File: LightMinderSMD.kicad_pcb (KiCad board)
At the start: 2 copper layers, 49.5 x 23 mm, 41 parts, among them J1 Conn_01x04_Female, J2 AVR-ISP-6, J3 Conn_01x04, J4 Conn_01x02_Female, Q1 Q_NPN_BEC, Q2 Q_NPN_BEC, Q3 STD35P6LLF6, U1 ATmega328P-AU, U2 LM3480-3.3, Y1 Crystal_GND24

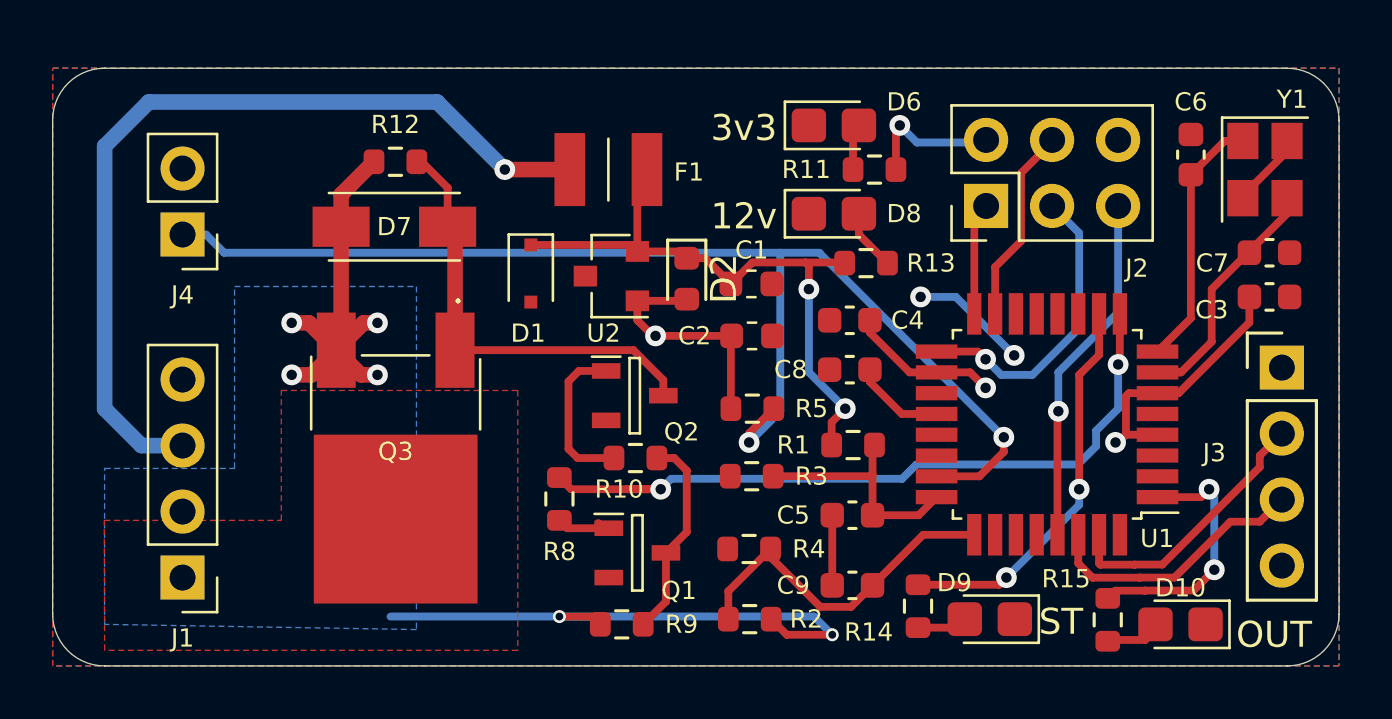
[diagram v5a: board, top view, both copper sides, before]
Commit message: Thermal management and Power plane modifications
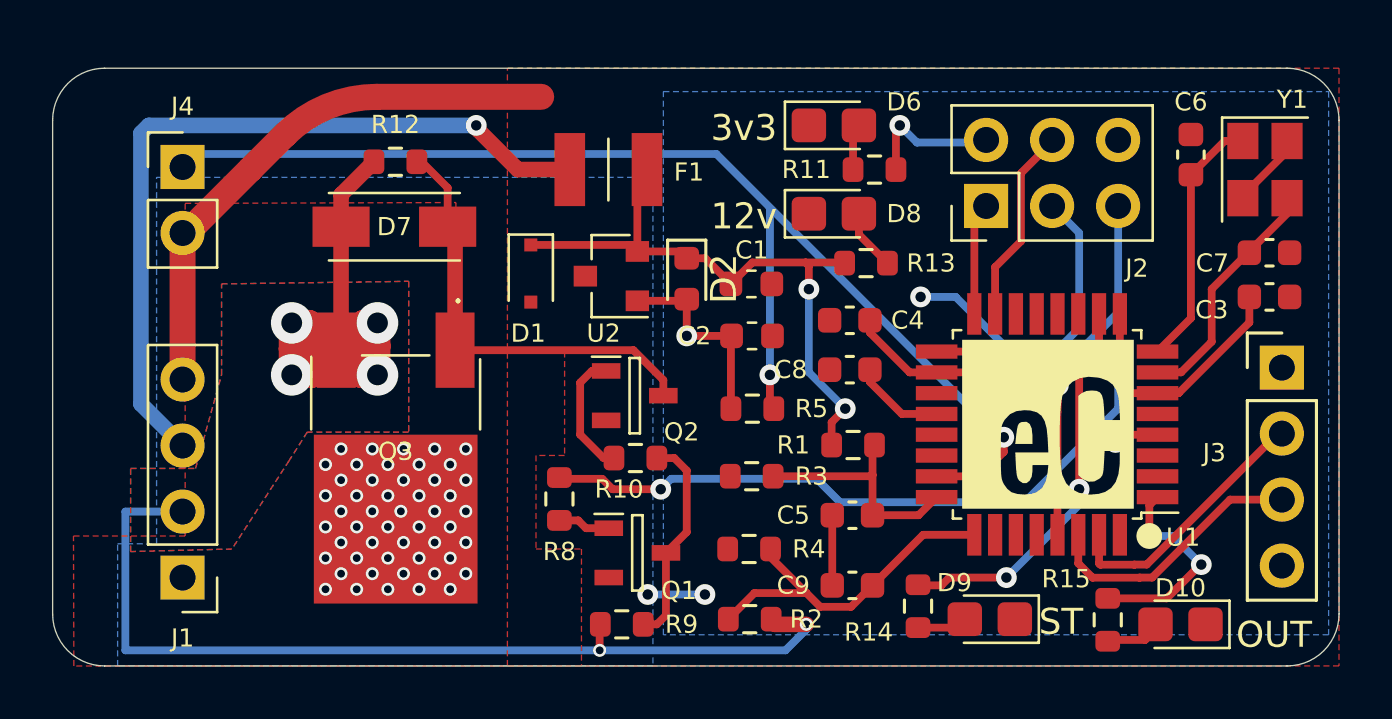
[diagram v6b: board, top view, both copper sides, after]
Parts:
- removed the G*** at (115.8, 90.7)
- added G***: LOGO, user:eC_Logo_6.5mm_Silkscreen, F.Cu at (131.3, 85.3)
- added G***: LOGO, user:LightMinderLogo_35mm, B.Cu at (119.8, 82.6)
- moved J4 2.60 mm to (98.0, 75.4), turned to 0 degrees
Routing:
- net Sidelight_GND: track 10.1 -> 33.7 mm, vias 2 -> 4
- net DippedBeam_12v: track 37.6 -> 60.2 mm
- net Sidelight_12v: track 33.4 -> 30.1 mm
- net 3v3: track 30.9 -> 29.0 mm
- net /Light_Out_LED: track 9.85 -> 8.22 mm
- net Net-(Q2-Pad1): track 6.11 -> 4.86 mm
- net /Sheet60CB0BEF/XTAL1: track 9.57 -> 8.70 mm
- net /Light_Out_Logic: track 28.1 -> 27.4 mm
- net Net-(D9-Pad2): track 2.68 -> 1.93 mm
- net Net-(Q1-Pad3): track 7.54 -> 8.27 mm
- net DippedBeam_Out: vias 0 -> 50
- added copper zone on F.Cu, net DippedBeam_12v
- added copper zone on B.Cu, net DippedBeam_Out
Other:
- board text added: "v0.4 PROTOTYPE 2021"
- board text removed: "v0.3 PROTOTYPE 2021"

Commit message: Layout Improvements and Added 3D models
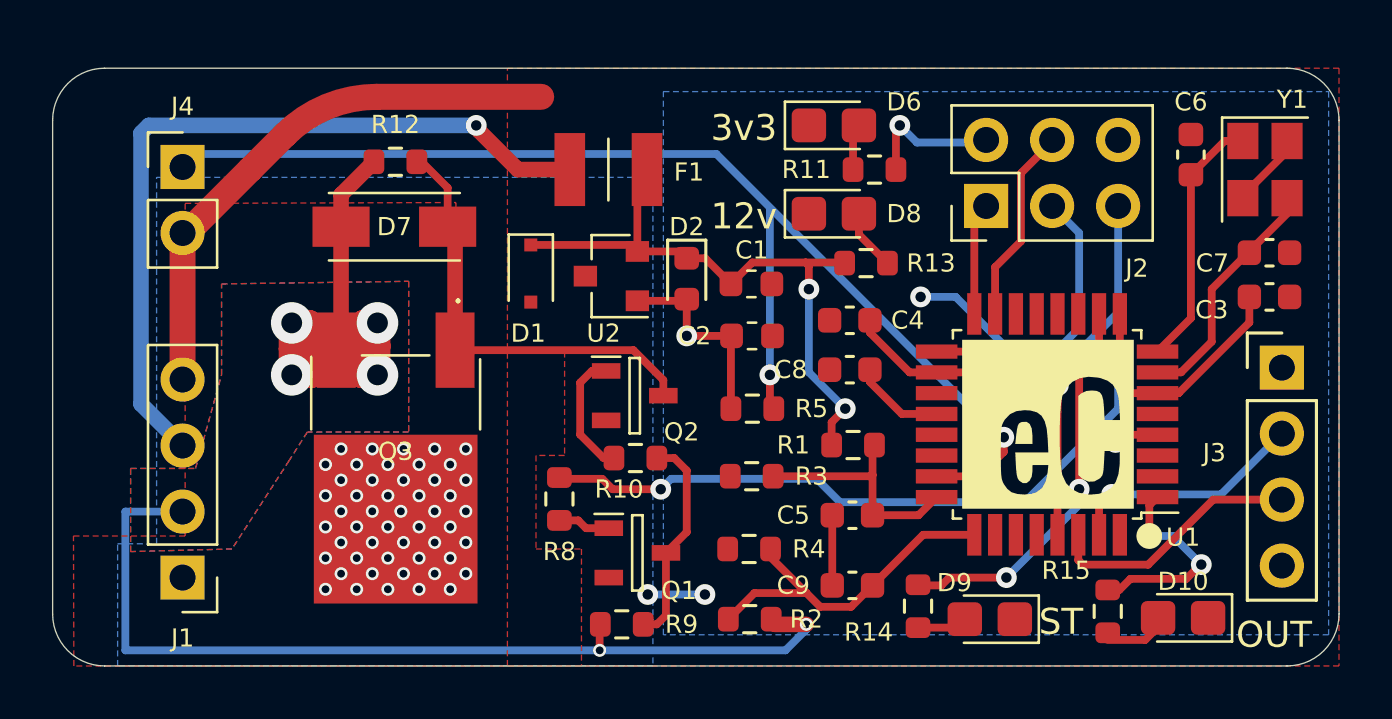
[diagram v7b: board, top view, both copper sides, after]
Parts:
- moved R15 0.33 mm to (133.6, 92.5)
- moved D10 0.27 mm to (136.5, 92.8)
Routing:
- net /TX: track 10.2 -> 9.27 mm, vias 0 -> 1
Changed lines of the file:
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@@
     (pad "32" smd rect locked (at -2.8 -4.25 270) (size 1.6 0.55) (layers "F.Cu" "F.Paste" "F.Mask")
       (net 30 "/Sheet60CB0BEF/2") (pinfunction "PD2") (pintype "bidirectional"))
-    (model "${KISYS3DMOD}/Package_QFP.3dshapes/TQFP-32_7x7mm_P0.8mm.wrl"
+    (model "C:/Program Files/KiCad/6.0/share/kicad/3dmodels//Package_QFP.3dshapes/TQFP-32_7x7mm_P0.8mm.wrl"
       (offset (xyz 0 0 0))
       (scale (xyz 1 1 1))
@@
     (pad "6" thru_hole oval locked (at 2.54 5.08 90) (size 1.7 1.7) (drill 1) (layers *.Cu *.Mask)
       (net 1 "Sidelight_GND") (pinfunction "GND") (pintype "passive"))
-    (model "${KISYS3DMOD}/Connector_PinHeader_2.54mm.3dshapes/PinHeader_2x03_P2.54mm_Vertical.wrl"
+    (model "${KISYS3DMOD}/Connector_PinHeader_2.54mm.3dshapes/PinHeader_2x03_P2.54mm_Vertical.wrl" hide
       (offset (xyz 0 0 0))
       (scale (xyz 1 1 1))
@@
     (pad "3" smd rect locked (at 2.286 3.25 180) (size 1.5 2.9) (layers "F.Cu" "F.Paste" "F.Mask")
       (net 4 "DippedBeam_12v"))
+    (model "${KICAD6_3DMODEL_DIR}/Package_TO_SOT_SMD.3dshapes/TO-252-2.step"
+      (offset (xyz 0 1.25 0))
+      (scale (xyz 1 1 1))
+      (rotate (xyz 0 0 -90))
+    )
   )
   (footprint "SamacSys_Parts:DO-214ACSMA" (layer "F.Cu")
@@
     (pad "2" smd rect locked (at 2.05 0 90) (size 1.55 2.2) (layers "F.Cu" "F.Paste" "F.Mask")
       (net 19 "Net-(D7-Pad2)") (pinfunction "A2") (pintype "passive"))
+    (model "${KIPRJMOD}/3D_Models/SMA.step"
+      (offset (xyz 0 0 0))
+      (scale (xyz 1 1 1))
+      (rotate (xyz 0 0 0))
+    )
   )
   (footprint "Connector_PinHeader_2.54mm:PinHeader_1x04_P2.54mm_Vertical" (layer "F.Cu")
@@
     (pad "4" thru_hole oval locked (at 0 7.62 180) (size 1.7 1.7) (drill 1) (layers *.Cu *.Mask)
       (net 1 "Sidelight_GND") (pinfunction "Pin_4") (pintype "passive"))
-    (model "${KISYS3DMOD}/Connector_PinHeader_2.54mm.3dshapes/PinHeader_1x04_P2.54mm_Vertical.wrl"
-      (offset (xyz 0 0 0))
+    (model "${KIPRJMOD}/3D_Models/KF128-2.54-4P.step"
+      (offset (xyz 0 -4 0))
       (scale (xyz 1 1 1))
-      (rotate (xyz 0 0 0))
+      (rotate (xyz 0 0 -90))
     )
   )
@@
     (pad "2" thru_hole oval locked (at 0 2.54) (size 1.7 1.7) (drill 1) (layers *.Cu *.Mask)
       (net 1 "Sidelight_GND") (pinfunction "Pin_2") (pintype "passive"))
-    (model "${KISYS3DMOD}/Connector_PinHeader_2.54mm.3dshapes/PinHeader_1x02_P2.54mm_Vertical.wrl"
-      (offset (xyz 0 0 0))
+    (model "${KIPRJMOD}/3D_Models/KF128-2.54-2P.step"
+      (offset (xyz 0 -1.25 0))
       (scale (xyz 1 1 1))
-      (rotate (xyz 0 0 0))
+      (rotate (xyz 0 0 90))
     )
   )
@@
     (pad "3" smd rect locked (at 1.1 0 90) (size 0.6 1.1) (layers "F.Cu" "F.Paste" "F.Mask")
       (net 19 "Net-(D7-Pad2)") (pinfunction "C") (pintype "passive"))
+    (model "${KICAD6_3DMODEL_DIR}/Package_TO_SOT_SMD.3dshapes/SOT-23.step"
+      (offset (xyz 0 0 0))
+      (scale (xyz 1 1 1))
+      (rotate (xyz 0 0 0))
+    )
   )
   (footprint "LED_SMD:LED_0805_2012Metric_Castellated" (layer "F.Cu")
@@
     (pad "2" smd roundrect locked (at 0.775 0) (size 0.9 0.95) (layers "F.Cu" "F.Paste" "F.Mask") (roundrect_rratio 0.25)
       (net 1 "Sidelight_GND") (pintype "passive"))
-    (model "${KISYS3DMOD}/Capacitor_SMD.3dshapes/C_0603_1608Metric.wrl"
+    (model "C:/Program Files/KiCad/6.0/share/kicad/3dmodels/Capacitor_SMD.3dshapes/C_0603_1608Metric.wrl"
       (offset (xyz 0 0 0))
       (scale (xyz 1 1 1))
@@
   )
   (footprint "Resistor_SMD:R_0603_1608Metric" (layer "F.Cu")
-    (at 133.6 92.825 -90)
+    (at 133.6 92.5 -90)
     (descr "Resistor SMD 0603 (1608 Metric), square (rectangular) end terminal, IPC_7351 nominal, (Body size source: IPC-SM-782 page 72, https://www.pcb-3d.com/wordpress/wp-content/uploads/ipc-sm-782a_amendment_1_and_2.pdf), generated with kicad-footprint-generator")
     (tags "resistor")
@@
   )
   (footprint "LED_SMD:LED_0805_2012Metric_Castellated" (layer "F.Cu")
-    (at 136.4 93 180)
+    (at 136.5 92.75 180)
     (descr "LED SMD 0805 (2012 Metric), castellated end terminal, IPC_7351 nominal, (Body size source: https://docs.google.com/spreadsheets/d/1BsfQQcO9C6DZCsRaXUlFlo91Tg2WpOkGARC1WS5S8t0/edit?usp=sharing), generated with kicad-footprint-generator")
     (tags "LED castellated")
@@
     (pad "3" smd rect locked (at 1.1 0 90) (size 0.6 1.1) (layers "F.Cu" "F.Paste" "F.Mask")
       (net 21 "Net-(Q1-Pad3)") (pinfunction "C") (pintype "passive"))
+    (model "${KICAD6_3DMODEL_DIR}/Package_TO_SOT_SMD.3dshapes/SOT-23.step"
+      (offset (xyz 0 0 0))
+      (scale (xyz 1 1 1))
+      (rotate (xyz 0 0 0))
+    )
   )
   (footprint "Package_TO_SOT_SMD:SOT-23" (layer "F.Cu")
@@
     (pad "4" thru_hole oval locked (at 0 7.62) (size 1.7 1.7) (drill 1) (layers *.Cu *.Mask)
       (net 16 "3v3") (pinfunction "Pin_4") (pintype "passive"))
-    (model "${KISYS3DMOD}/Connector_PinHeader_2.54mm.3dshapes/PinHeader_1x04_P2.54mm_Vertical.wrl"
+    (model "${KISYS3DMOD}/Connector_PinHeader_2.54mm.3dshapes/PinHeader_1x04_P2.54mm_Vertical.wrl" hide
       (offset (xyz 0 0 0))
       (scale (xyz 1 1 1))
@@
     (pad "2" smd rect locked (at 1.485 0) (size 1.18 2.81) (layers "F.Cu" "F.Paste" "F.Mask")
       (net 11 "/12vFused") (pintype "passive"))
+    (model "${KICAD6_3DMODEL_DIR}/Fuse.3dshapes/Fuse_0805_2012Metric.step"
+      (offset (xyz 0 0 0))
+      (scale (xyz 1 1 1))
+      (rotate (xyz 0 0 0))
+    )
+    (model "${KICAD6_3DMODEL_DIR}/Fuse.3dshapes/Fuse_1206_3216Metric.step"
+      (offset (xyz 0 0 0))
+      (scale (xyz 1 1 1))
+      (rotate (xyz 0 0 0))
+    )
   )
   (footprint "Capacitor_SMD:C_0603_1608Metric" (layer "F.Cu")
@@
     (property "Sheetname" "")
     (attr smd)
-    (fp_text reference "D2" (at 0 -1.43 90) (layer "F.SilkS")
-      (effects (font (size 1 1) (thickness 0.15)))
+    (fp_text reference "D2" (at -2 0 180) (layer "F.SilkS")
+      (effects (font (size 0.7 0.7) (thickness 0.1)))
     )
     (fp_text value "D_Schottky" (at 0 1.43 90) (layer "F.Fab")
@@
   (segment (start 140.5 77.2) (end 137.600011 80.099989) (width 0.3) (layer "F.Cu") (net 8))
   (segment (start 137.600011 80.099989) (end 137.600011 82.124991) (width 0.3) (layer "F.Cu") (net 8))
-  (segment (start 140.14 85.66) (end 135.100022 90.699978) (width 0.3) (layer "F.Cu") (net 9))
-  (segment (start 134.621002 90.704) (end 133.316 90.704) (width 0.3) (layer "F.Cu") (net 9))
-  (segment (start 134.625024 90.699978) (end 134.621002 90.704) (width 0.3) (layer "F.Cu") (net 9))
-  (segment (start 133.266 90.654) (end 133.266 89.554) (width 0.3) (layer "F.Cu") (net 9))
-  (segment (start 133.316 90.704) (end 133.266 90.654) (width 0.3) (layer "F.Cu") (net 9))
-  (segment (start 140.3 85.66) (end 140.14 85.66) (width 0.3) (layer "F.Cu") (net 9))
-  (segment (start 135.100022 90.699978) (end 134.625024 90.699978) (width 0.3) (layer "F.Cu") (net 9))
-  (segment (start 134.832135 91.199989) (end 135.306439 91.199989) (width 0.3) (layer "F.Cu") (net 10))
-  (segment (start 132.466 90.654) (end 133.016012 91.204012) (width 0.3) (layer "F.Cu") (net 10))
-  (segment (start 134.828112 91.204012) (end 134.832135 91.199989) (width 0.3) (layer "F.Cu") (net 10))
-  (segment (start 135.306439 91.199989) (end 138.306428 88.2) (width 0.3) (layer "F.Cu") (net 10))
-  (segment (start 138.306428 88.2) (end 140.3 88.2) (width 0.3) (layer "F.Cu") (net 10))
-  (segment (start 132.466 89.554) (end 132.466 90.654) (width 0.3) (layer "F.Cu") (net 10))
-  (segment (start 133.016012 91.204012) (end 134.828112 91.204012) (width 0.3) (layer "F.Cu") (net 10))
+  (segment (start 133.266 89.554) (end 133.266 88.484) (width 0.3) (layer "F.Cu") (net 9))
+  (segment (start 133.266 88.484) (end 133.75 88) (width 0.3) (layer "F.Cu") (net 9))
+  (via (at 133.75 88) (size 0.8) (drill 0.4) (layers "F.Cu" "B.Cu") (net 9))
+  (segment (start 133.75 88) (end 137.96 88) (width 0.3) (layer "B.Cu") (net 9))
+  (segment (start 137.96 88) (end 140.3 85.66) (width 0.3) (layer "B.Cu") (net 9))
+  (segment (start 137.65997 88.2) (end 140.3 88.2) (width 0.3) (layer "F.Cu") (net 10))
+  (segment (start 132.641489 90.703511) (end 135.156459 90.703511) (width 0.3) (layer "F.Cu") (net 10))
+  (segment (start 132.466 89.554) (end 132.466 90.528022) (width 0.3) (layer "F.Cu") (net 10))
+  (segment (start 132.466 90.528022) (end 132.641489 90.703511) (width 0.3) (layer "F.Cu") (net 10))
+  (segment (start 135.156459 90.703511) (end 137.65997 88.2) (width 0.3) (layer "F.Cu") (net 10))
   (segment (start 123.44999 79.07499) (end 121.97499 79.07499) (width 0.3) (layer "F.Cu") (net 11))
   (segment (start 111.4 78.4) (end 115.25 78.4) (width 0.3) (layer "F.Cu") (net 11))
@@
   (segment (start 132.5 88.4) (end 129.7 91.2) (width 0.3) (layer "B.Cu") (net 14))
   (segment (start 132.5 87.8) (end 132.5 88.4) (width 0.3) (layer "B.Cu") (net 14))
+  (segment (start 134.471468 91.25) (end 134.046468 91.675) (width 0.3) (layer "F.Cu") (net 15))
   (segment (start 137.2 90.7) (end 137.172414 90.7) (width 0.3) (layer "F.Cu") (net 15))
-  (segment (start 135.872414 92) (end 133.6 92) (width 0.3) (layer "F.Cu") (net 15))
   (segment (start 135.2 88.42) (end 135.516 88.104) (width 0.3) (layer "F.Cu") (net 15))
   (segment (start 135.2 89.6) (end 135.2 88.42) (width 0.3) (layer "F.Cu") (net 15))
-  (segment (start 137.172414 90.7) (end 135.872414 92) (width 0.3) (layer "F.Cu") (net 15))
+  (segment (start 134.046468 91.675) (end 133.6 91.675) (width 0.3) (layer "F.Cu") (net 15))
+  (segment (start 137.172414 90.7) (end 136.622414 91.25) (width 0.3) (layer "F.Cu") (net 15))
+  (segment (start 136.622414 91.25) (end 134.471468 91.25) (width 0.3) (layer "F.Cu") (net 15))
   (via (at 137.2 90.7) (size 0.8) (drill 0.4) (layers "F.Cu" "B.Cu") (net 15))
   (via (at 135.2 89.6) (size 0.8) (drill 0.4) (layers "F.Cu" "B.Cu") (net 15))

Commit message: ICSP Typo Fix
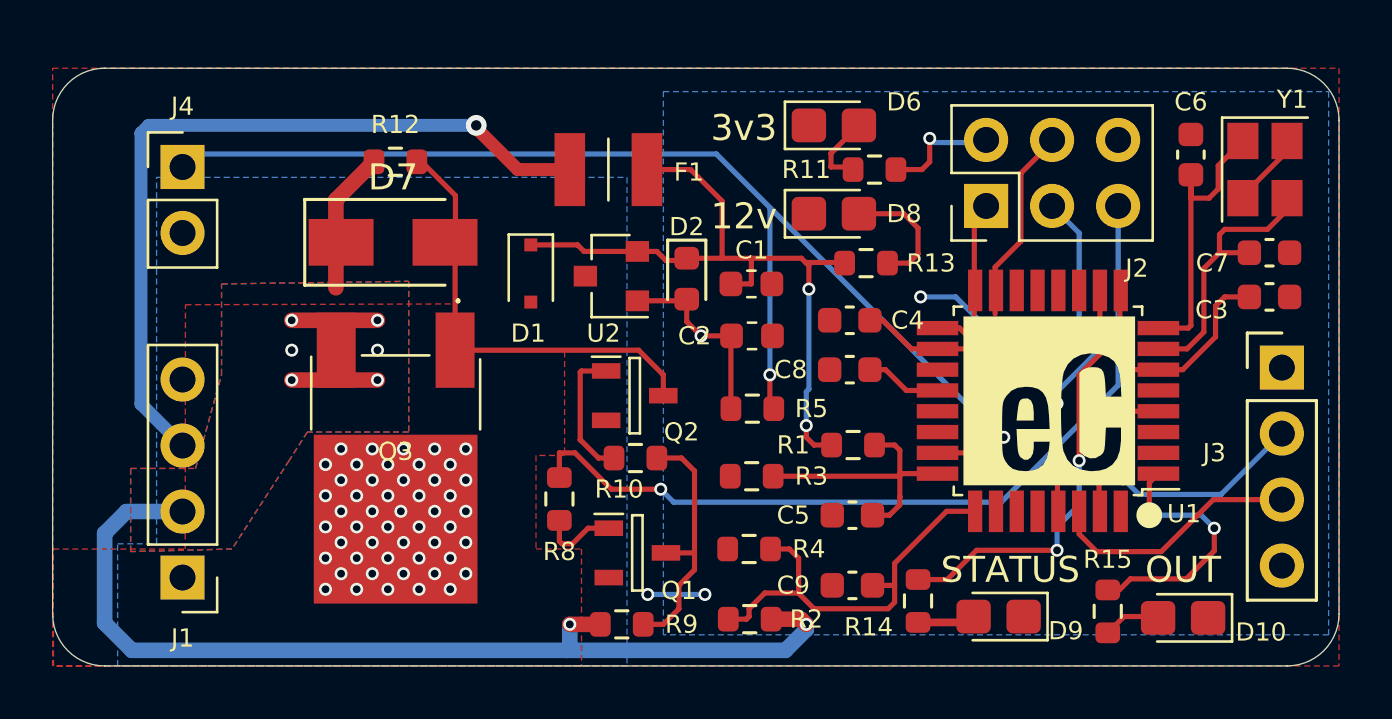
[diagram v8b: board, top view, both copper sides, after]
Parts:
- added G***: LOGO, user:eC_Logo_6.5mm_Silkscreen, B.Cu at (139.2, 74.9)
- D7: footprint SamacSys_Parts:DO-214ACSMA -> Diode_SMD:D_SMA
- moved U1 0.90 mm to (131.3, 84.4)
- moved G*** 0.90 mm to (131.3, 84.4)
- moved D7 0.60 mm to (106.1, 78.3)
- moved G*** 0.43 mm to (119.4, 82.6)
- moved D9 0.35 mm to (129.4, 92.7)
- moved R14 0.20 mm to (126.3, 92.1)
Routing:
- net Sidelight_GND: track 33.7 -> 9.28 mm
- net DippedBeam_12v: track 60.2 -> 50.1 mm, vias 6 -> 8
- net /12vFused: track 24.2 -> 27.6 mm
- net /dipped_beam_ref: track 13.5 -> 16.2 mm
- net Net-(D8-Pad2): track 2.36 -> 4.82 mm
- net 3v3: track 29.0 -> 27.0 mm
- net /Light_Out_LED: track 8.09 -> 10.0 mm
- net /light_ref: track 47.6 -> 46.0 mm
- net Net-(Q1-Pad3): track 8.27 -> 9.93 mm
- net /Sheet60CB0BEF/XTAL2: track 9.87 -> 11.4 mm
- net /Sheet60CB0BEF/XTAL1: track 8.70 -> 10.2 mm
- net /Error_LED: track 15.2 -> 16.6 mm
- net /batt_voltage_ref: track 9.33 -> 10.7 mm
- net /Light_Out_Logic: track 27.4 -> 28.7 mm
- net Net-(D6-Pad2): track 1.79 -> 2.85 mm
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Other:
- board text added: "ICSP"
- board text added: "STATUS"
- board text added: "Serial"
- board text added: "v0.4 PROTOTYPE 2022"
- board text removed: "ISCP"
- board text removed: "ST"
- board text removed: "Serial Port"
- board text removed: "v0.4 PROTOTYPE 2021"
